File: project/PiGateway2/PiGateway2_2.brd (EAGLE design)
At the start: 65 x 30 mm, 14 parts

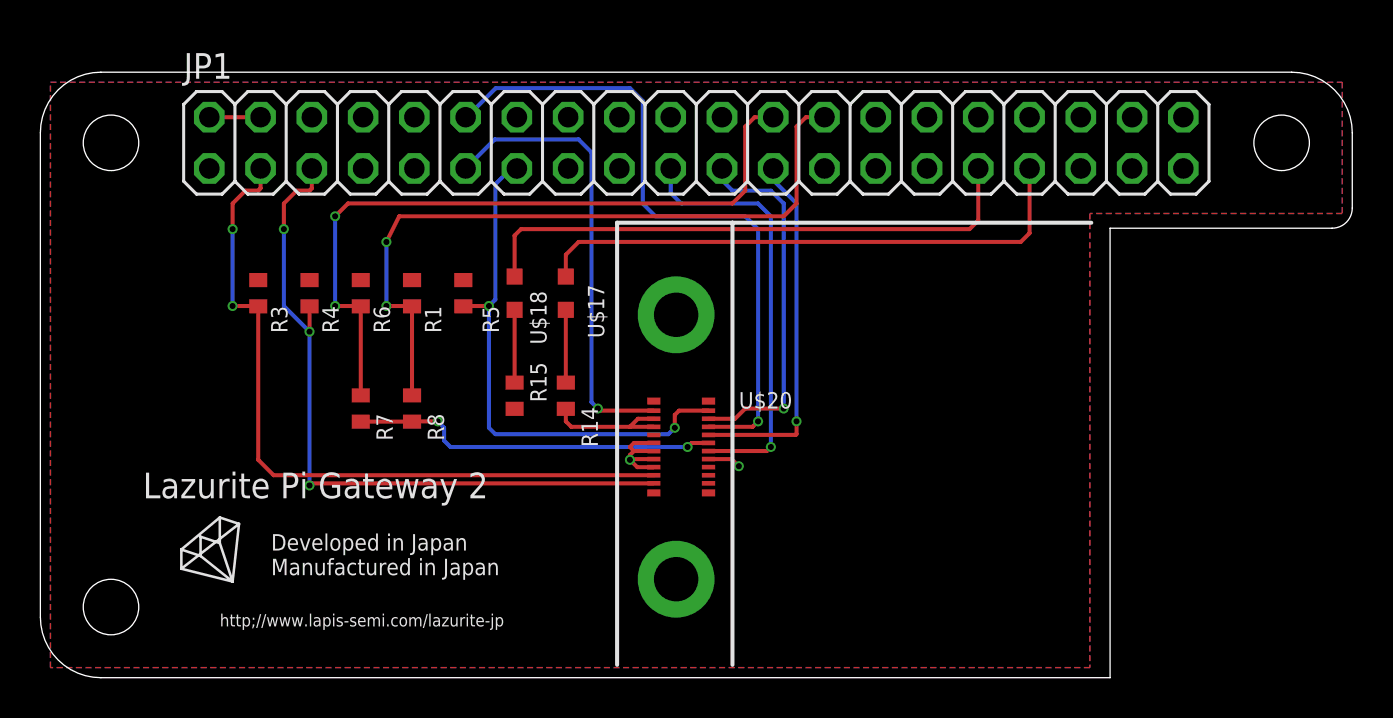
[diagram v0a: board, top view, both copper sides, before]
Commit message: update project of pump monitoring incl. sound and motion.
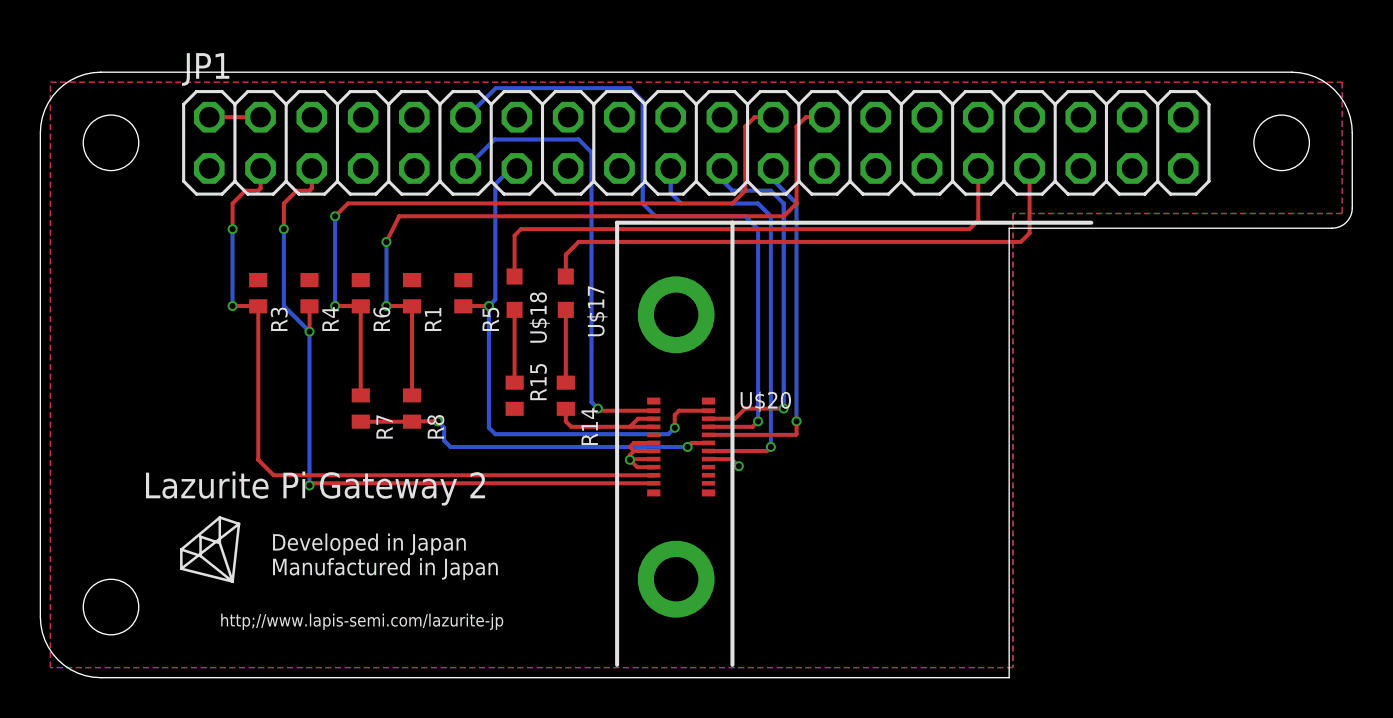
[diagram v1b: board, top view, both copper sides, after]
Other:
- outline, holes or cut-outs redrawn
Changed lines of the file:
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@@
 <plain>
 <wire x1="0" y1="3" x2="3" y2="0" width="0" layer="20" curve="90"/>
-<wire x1="3" y1="0" x2="53" y2="0" width="0" layer="20"/>
-<wire x1="53" y1="0" x2="53" y2="22.27" width="0" layer="20"/>
-<wire x1="53" y1="22.27" x2="64" y2="22.27" width="0" layer="20"/>
+<wire x1="3" y1="0" x2="48" y2="0" width="0" layer="20"/>
+<wire x1="48" y1="0" x2="48" y2="22.27" width="0" layer="20"/>
+<wire x1="48" y1="22.27" x2="64" y2="22.27" width="0" layer="20"/>
 <wire x1="64" y1="22.27" x2="65" y2="23.27" width="0" layer="20" curve="90"/>
 <wire x1="65" y1="23.27" x2="65" y2="27" width="0" layer="20"/>
@@
 <vertex x="64.5" y="29.5"/>
 <vertex x="64.5" y="23"/>
-<vertex x="52" y="23"/>
-<vertex x="52" y="0.5"/>
+<vertex x="48.19" y="23"/>
+<vertex x="48.19" y="0.5"/>
 <vertex x="0.5" y="0.5"/>
 </polygon>
@@
 <vertex x="64.5" y="29.5"/>
 <vertex x="64.5" y="23"/>
-<vertex x="52" y="23"/>
-<vertex x="52" y="0.5"/>
+<vertex x="48.19" y="23"/>
+<vertex x="48.19" y="0.5"/>
 <vertex x="0.5" y="0.5"/>
 </polygon>
